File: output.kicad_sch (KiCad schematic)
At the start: 40 parts, among them J1 SMA, J2 SMA, J3 SMA, J4 SMA, T1 MABA-007159-000000, T2 MABA-007159-000000, U11 74LVC1G240, U12 74LVC1G125, U13 TS5A63157DBV

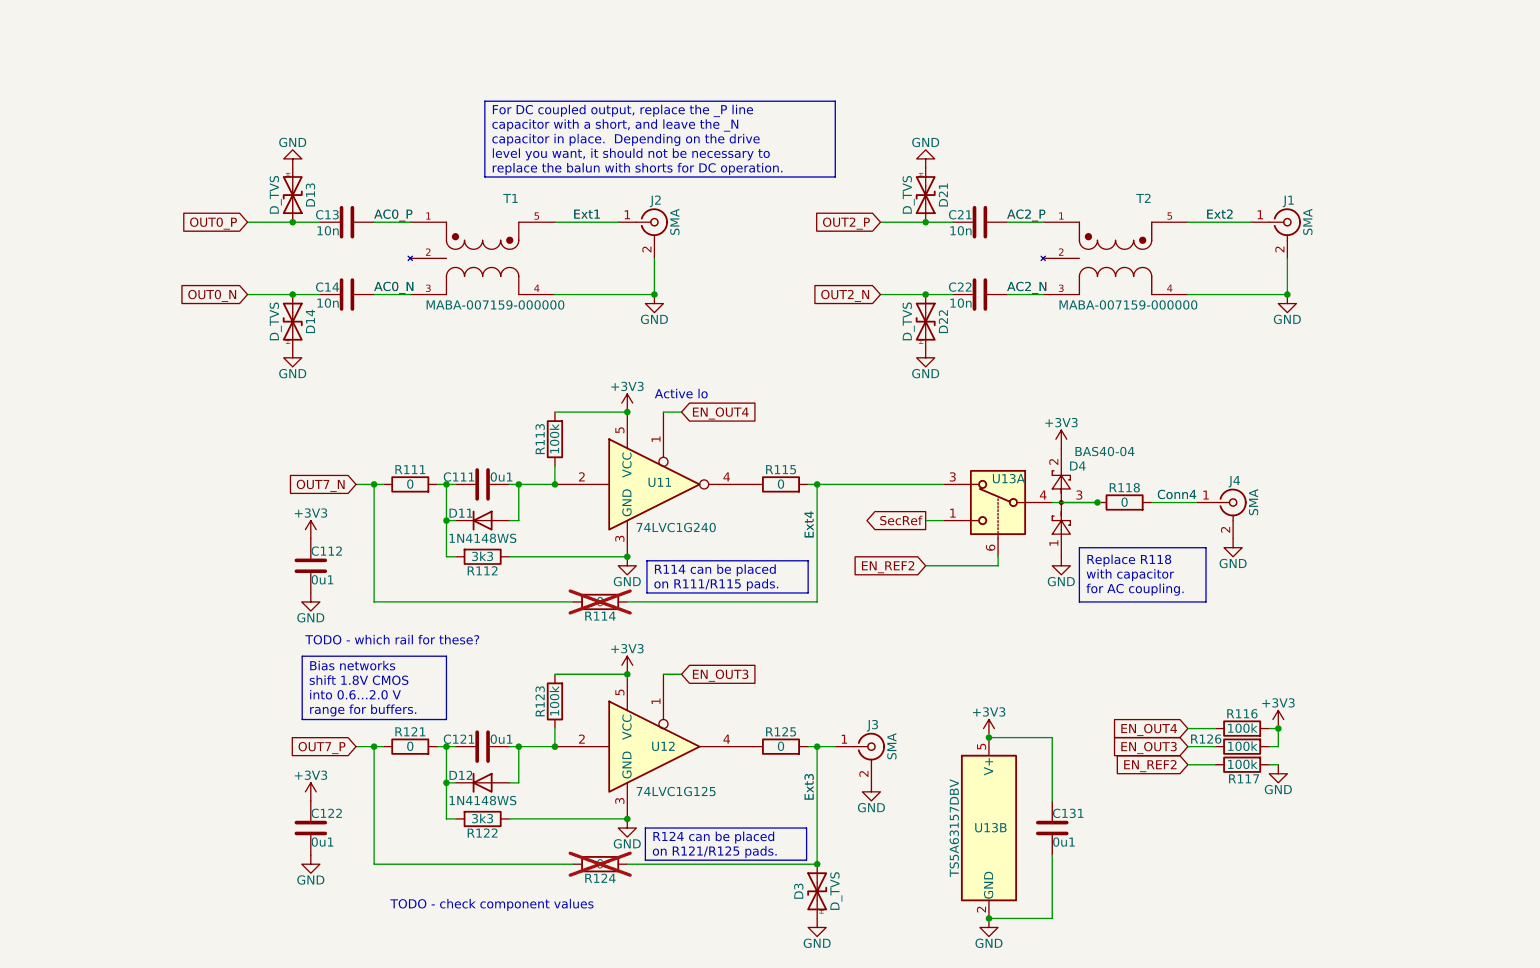
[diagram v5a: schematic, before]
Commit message: Supercap is back
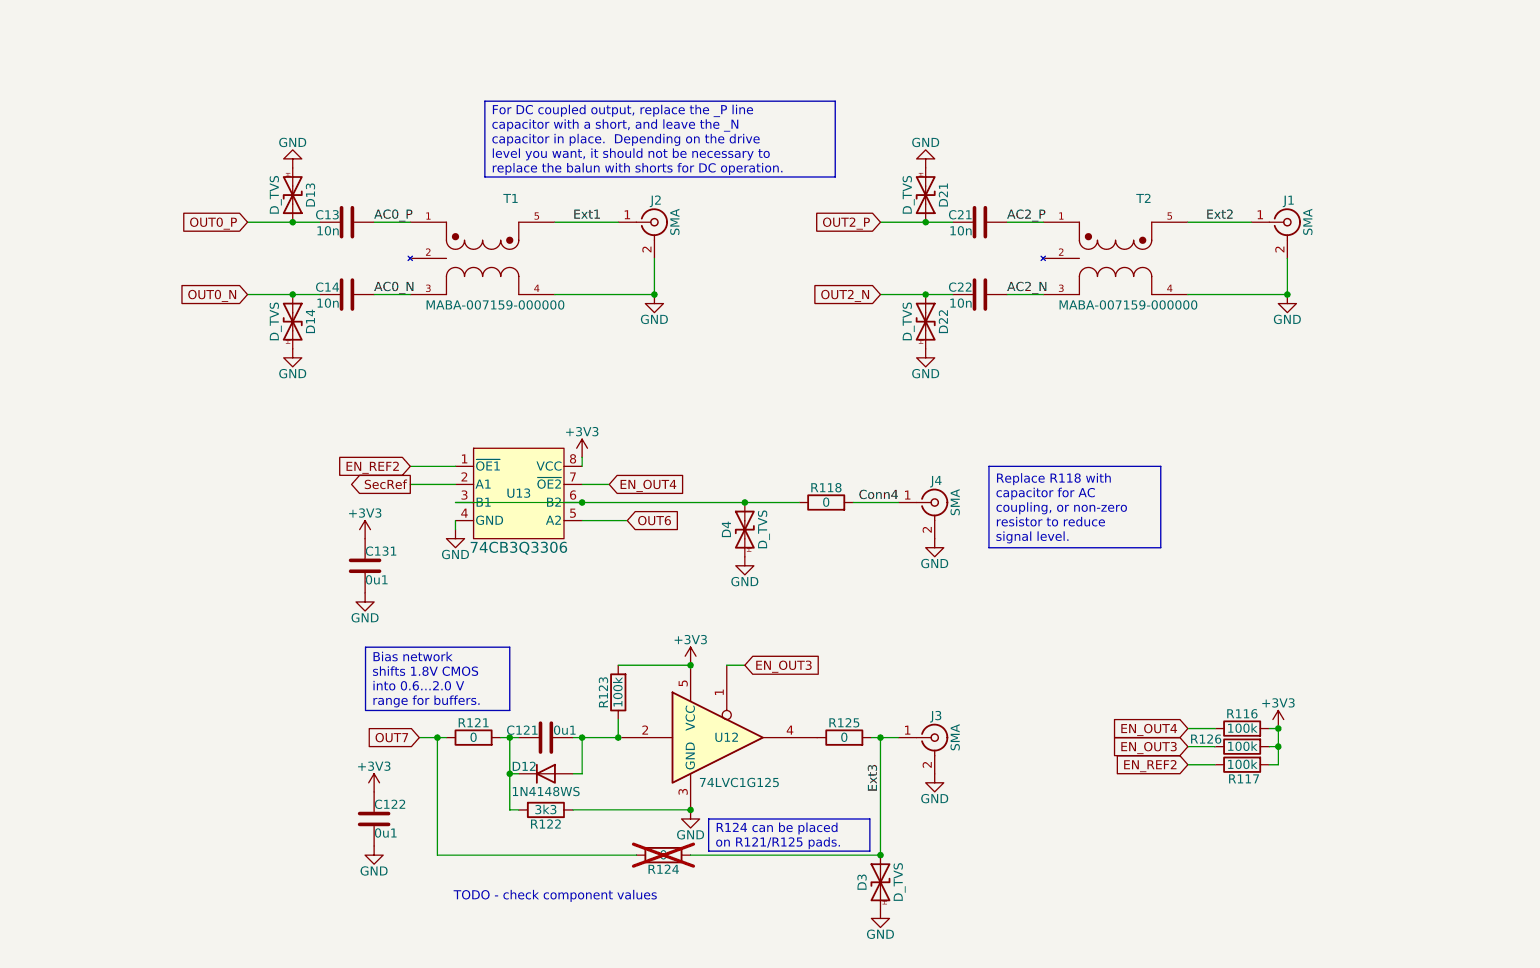
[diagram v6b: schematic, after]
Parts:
- removed C111, C112: 0u1, Capacitor_SMD:C_0402_1005Metric, symbol Device:C
- removed D11: 1N4148WS, Diode_SMD:D_SOD-323, symbol Diode:1N4148WS
- removed D4: BAS40-04, Package_TO_SOT_SMD:SOT-23, symbol Diode:BAS40-04
- removed R111, R114, R115: 0, Resistor_SMD:R_0603_1608Metric, symbol Device:R
- removed R112: 3k3, Resistor_SMD:R_0402_1005Metric, symbol Device:R
- removed R113: 100k, Resistor_SMD:R_0402_1005Metric, symbol Device:R
- removed U11: 74LVC1G240, Package_TO_SOT_SMD:SOT-23-5, symbol 74xGxx:74LVC1G240
- removed unit 2 of U13
- added D4: D_TVS, Parts:HHS_0402, symbol Parts:D_TVS
- U13: value TS5A63157DBV -> 74CB3Q3306; footprint Package_TO_SOT_SMD:SOT-23-6 -> Package_SO:VSSOP-8_2.3x2mm_P0.5mm; symbol Analog_Switch:TS5A63157DBV -> Parts:74CB3Q3306; now in the parts list
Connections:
- net Ext4 is gone; now on an unnamed net: U13.3 (B1)
- net +3V3: now also R117.2, U13.8 (VCC)
- net EN_OUT4: now also U13.7 (~{OE2})
- net EN_REF2: now also U13.1 (~{OE1}); no longer U13.6
- net GND: now also U13.4 (GND), D4.2 (A2); no longer R117.2
- net SecRef: now also U13.2 (A1); no longer U13.1
- net at R118.1: now also U13.6 (B2), D4.1 (A1); no longer U13.4
- net OUT7_P renamed OUT7
- new net OUT6: U13.5 (A2)
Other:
- note removed: "Active lo"
- note removed: "TODO - which rail for these?"
- moved on the sheet: C121, C122, C131, D12, D3, J3, J4, R118, R121, R122, R123, R124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

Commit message: Down to the dregs and clean-ups.
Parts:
- C13, C14, C21, C22: JLCPCB (none) -> C15195
- C76: renamed from C131; JLCPCB (none) -> C307331
- C77: renamed from C122; JLCPCB (none) -> C307331
- C78: renamed from C121; JLCPCB (none) -> C307331
- D12: JLCPCB (none) -> C2128
- D13, D14, D21, D22, D3, D4, U13: now left out of the parts list
- R74: renamed from R121; JLCPCB (none) -> C21189
- R75: renamed from R118; JLCPCB (none) -> C21189
- R76: renamed from R122; JLCPCB (none) -> C25890
- R77: renamed from R123; JLCPCB (none) -> C25741
- R78: renamed from R125; JLCPCB (none) -> C21189
- R79: renamed from R116; JLCPCB (none) -> C25741
- R80: renamed from R126; JLCPCB (none) -> C25741
- R84: renamed from R117; JLCPCB (none) -> C25741
- T1, T2: JLCPCB (none) -> C350943
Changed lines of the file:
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@@
 		(on_board yes)
 		(dnp no)
-		(property "Reference" "C121"
+		(property "Reference" "C78"
 			(at 128.524 125.476 90)
 			(effects
@@
 			)
 		)
-		(property "JLCPCB" ""
+		(property "JLCPCB" "C307331"
 			(at 129.54 125.73 0)
 			(effects
@@
 			(project "gpsref"
 				(path "/3160ff17-81c2-4674-af97-e8d9acaf6b65/26994282-45a2-461a-b033-dde2ded4d8ff"
-					(reference "C121")
+					(reference "C78")
 					(unit 1)
 				)
@@
 		(unit 1)
 		(exclude_from_sim no)
-		(in_bom yes)
+		(in_bom no)
 		(on_board yes)
 		(dnp no)
@@
 		(unit 1)
 		(exclude_from_sim no)
-		(in_bom yes)
+		(in_bom no)
 		(on_board yes)
 		(dnp no)
@@
 			)
 		)
-		(property "JLCPCB" ""
+		(property "JLCPCB" "C15195"
 			(at 101.6 53.34 0)
 			(effects
@@
 		(unit 1)
 		(exclude_from_sim no)
-		(in_bom yes)
+		(in_bom no)
 		(on_board yes)
 		(dnp no)
@@
 			)
 		)
-		(property "JLCPCB" ""
+		(property "JLCPCB" "C15195"
 			(at 190.5 63.5 0)
 			(effects
@@
 			)
 		)
+		(property "JLCPCB" "C350943"
+			(at 209.55 58.42 0)
+			(effects
+				(font
+					(size 1.27 1.27)
+				)
+				(hide yes)
+			)
+		)
 		(pin "3"
 		)
@@
 		(on_board yes)
 		(dnp no)
-		(property "Reference" "R122"
+		(property "Reference" "R76"
 			(at 129.54 137.922 90)
 			(effects
@@
 			)
 		)
-		(property "JLCPCB" ""
+		(property "JLCPCB" "C25890"
 			(at 129.54 135.89 0)
 			(effects
@@
 			(project "gpsref"
 				(path "/3160ff17-81c2-4674-af97-e8d9acaf6b65/26994282-45a2-461a-b033-dde2ded4d8ff"
-					(reference "R122")
+					(reference "R76")
 					(unit 1)
 				)
@@
 			)
 		)
+		(property "JLCPCB" "C350943"
+			(at 120.65 58.42 0)
+			(effects
+				(font
+					(size 1.27 1.27)
+				)
+				(hide yes)
+			)
+		)
 		(pin "3"
 		)
@@
 		(on_board yes)
 		(dnp no)
-		(property "Reference" "R117"
+		(property "Reference" "R84"
 			(at 227.584 131.572 90)
 			(effects
@@
 			)
 		)
-		(property "Datasheet" "Not sure about value."
+		(property "Datasheet" "~"
 			(at 227.33 129.54 0)
 			(effects
@@
 			)
 		)
-		(property "JLCPCB" ""
+		(property "JLCPCB" "C25741"
 			(at 227.33 129.54 0)
 			(effects
@@
 			(project "gpsref"
 				(path "/3160ff17-81c2-4674-af97-e8d9acaf6b65/26994282-45a2-461a-b033-dde2ded4d8ff"
-					(reference "R117")
+					(reference "R84")
 					(unit 1)
 				)
@@
 		(on_board yes)
 		(dnp no)
-		(property "Reference" "C122"
+		(property "Reference" "C77"
 			(at 105.41 135.89 0)
 			(effects
@@
 			)
 		)
+		(property "JLCPCB" "C307331"
+			(at 105.41 137.16 0)
+			(effects
+				(font
+					(size 1.27 1.27)
+				)
+				(hide yes)
+			)
+		)
 		(pin "1"
 		)
@@
 			(project "gpsref"
 				(path "/3160ff17-81c2-4674-af97-e8d9acaf6b65/26994282-45a2-461a-b033-dde2ded4d8ff"
-					(reference "C122")
+					(reference "C77")
 					(unit 1)
 				)
@@
 		(on_board yes)
 		(dnp no)
-		(property "Reference" "R125"
+		(property "Reference" "R78"
 			(at 171.45 123.698 90)
 			(effects
@@
 			)
 		)
-		(property "Datasheet" "Not sure about value."
+		(property "Datasheet" "~"
 			(at 171.45 125.73 0)
 			(effects
@@
 			)
 		)
-		(property "JLCPCB" ""
+		(property "JLCPCB" "C21189"
 			(at 171.45 125.73 0)
 			(effects
@@
 			(project "gpsref"
 				(path "/3160ff17-81c2-4674-af97-e8d9acaf6b65/26994282-45a2-461a-b033-dde2ded4d8ff"
-					(reference "R125")
+					(reference "R78")
 					(unit 1)
 				)
@@
 		(unit 1)
 		(exclude_from_sim no)
-		(in_bom yes)
+		(in_bom no)
 		(on_board yes)
 		(dnp no)
@@
 		(on_board yes)
 		(dnp no)
-		(property "Reference" "R116"
+		(property "Reference" "R79"
 			(at 227.33 122.428 90)
 			(effects
@@
 			)
 		)
-		(property "Datasheet" "Not sure about value."
+		(property "Datasheet" "~"
 			(at 227.33 124.46 0)
 			(effects
@@
 			)
 		)
-		(property "JLCPCB" ""
+		(property "JLCPCB" "C25741"
 			(at 227.33 124.46 0)
 			(effects
@@
 			(project "gpsref"
 				(path "/3160ff17-81c2-4674-af97-e8d9acaf6b65/26994282-45a2-461a-b033-dde2ded4d8ff"
-					(reference "R116")
+					(reference "R79")
 					(unit 1)
 				)
@@
 			)
 		)
-		(property "JLCPCB" ""
+		(property "JLCPCB" "C15195"
 			(at 101.6 63.5 0)
 			(effects
@@
 		(on_board yes)
 		(dnp no)
-		(property "Reference" "C131"
+		(property "Reference" "C76"
 			(at 104.14 100.33 0)
 			(effects
@@
 			)
 		)
+		(property "JLCPCB" "C307331"
+			(at 104.14 101.6 0)
+			(effects
+				(font
+					(size 1.27 1.27)
+				)
+				(hide yes)
+			)
+		)
 		(pin "1"
 		)
@@
 			(project "gpsref"
 				(path "/3160ff17-81c2-4674-af97-e8d9acaf6b65/26994282-45a2-461a-b033-dde2ded4d8ff"
-					(reference "C131")
+					(reference "C76")
 					(unit 1)
 				)
@@
 		(unit 1)
 		(exclude_from_sim no)
-		(in_bom yes)
+		(in_bom no)
 		(on_board yes)
 		(dnp no)
@@
 		(unit 1)
 		(exclude_from_sim no)
-		(in_bom yes)
+		(in_bom no)
 		(on_board yes)
 		(dnp no)
@@
 		(on_board yes)
 		(dnp no)
-		(property "Reference" "R118"
+		(property "Reference" "R75"
 			(at 168.91 90.678 90)
 			(effects
@@
 			)
 		)
-		(property "Datasheet" "Not sure about value."
+		(property "Datasheet" "~"
 			(at 168.91 92.71 0)
 			(effects
@@
 			)
 		)
-		(property "JLCPCB" ""
+		(property "JLCPCB" "C21189"
 			(at 168.91 92.71 0)
 			(effects
@@
 			(project "gpsref"
 				(path "/3160ff17-81c2-4674-af97-e8d9acaf6b65/26994282-45a2-461a-b033-dde2ded4d8ff"
-					(reference "R118")
+					(reference "R75")
 					(unit 1)
 				)
@@
 		(unit 1)
 		(exclude_from_sim no)
-		(in_bom yes)
+		(in_bom no)
 		(on_board yes)
 		(dnp no)
@@
 		(on_board yes)
 		(dnp no)
-		(property "Reference" "R121"
+		(property "Reference" "R74"
 			(at 119.38 123.698 90)
 			(effects
@@
 			)
 		)
-		(property "Datasheet" "Not sure about value."
+		(property "Datasheet" "~"
 			(at 119.38 125.73 0)
 			(effects
@@
 			)
 		)
-		(property "JLCPCB" ""
+		(property "JLCPCB" "C21189"
 			(at 119.38 125.73 0)
 			(effects
@@
 			(project "gpsref"
 				(path "/3160ff17-81c2-4674-af97-e8d9acaf6b65/26994282-45a2-461a-b033-dde2ded4d8ff"
-					(reference "R121")
+					(reference "R74")
 					(unit 1)
 				)
@@
 			)
 		)
-		(property "JLCPCB" ""
+		(property "JLCPCB" "C15195"
 			(at 190.5 53.34 0)
 			(effects
@@
 		(on_board yes)
 		(dnp no)
-		(property "Reference" "R123"
+		(property "Reference" "R77"
 			(at 137.668 119.38 90)
 			(effects
@@
 			)
 		)
-		(property "Datasheet" "Not sure about value."
+		(property "Datasheet" "~"
 			(at 139.7 119.38 0)
 			(effects
@@
 			)
 		)
-		(property "JLCPCB" ""
+		(property "JLCPCB" "C25741"
 			(at 139.7 119.38 0)
 			(effects
@@
 			(project "gpsref"
 				(path "/3160ff17-81c2-4674-af97-e8d9acaf6b65/26994282-45a2-461a-b033-dde2ded4d8ff"
-					(reference "R123")
+					(reference "R77")
 					(unit 1)
 				)
@@
 			)
 		)
+		(property "JLCPCB" "C2128"
+			(at 129.54 130.81 0)
+			(effects
+				(font
+					(size 1.27 1.27)
+				)
+				(hide yes)
+			)
+		)
 		(pin "2"
 		)
@@
 		(on_board yes)
 		(dnp no)
-		(property "Reference" "R126"
+		(property "Reference" "R80"
 			(at 222.25 125.984 90)
 			(effects
@@
 			)
 		)
-		(property "Datasheet" "Not sure about value."
+		(property "Datasheet" "~"
 			(at 227.33 127 0)
 			(effects
@@
 			)
 		)
-		(property "JLCPCB" ""
+		(property "JLCPCB" "C25741"
 			(at 227.33 127 0)
 			(effects
@@
 			(project "gpsref"
 				(path "/3160ff17-81c2-4674-af97-e8d9acaf6b65/26994282-45a2-461a-b033-dde2ded4d8ff"
-					(reference "R126")
+					(reference "R80")
 					(unit 1)
 				)

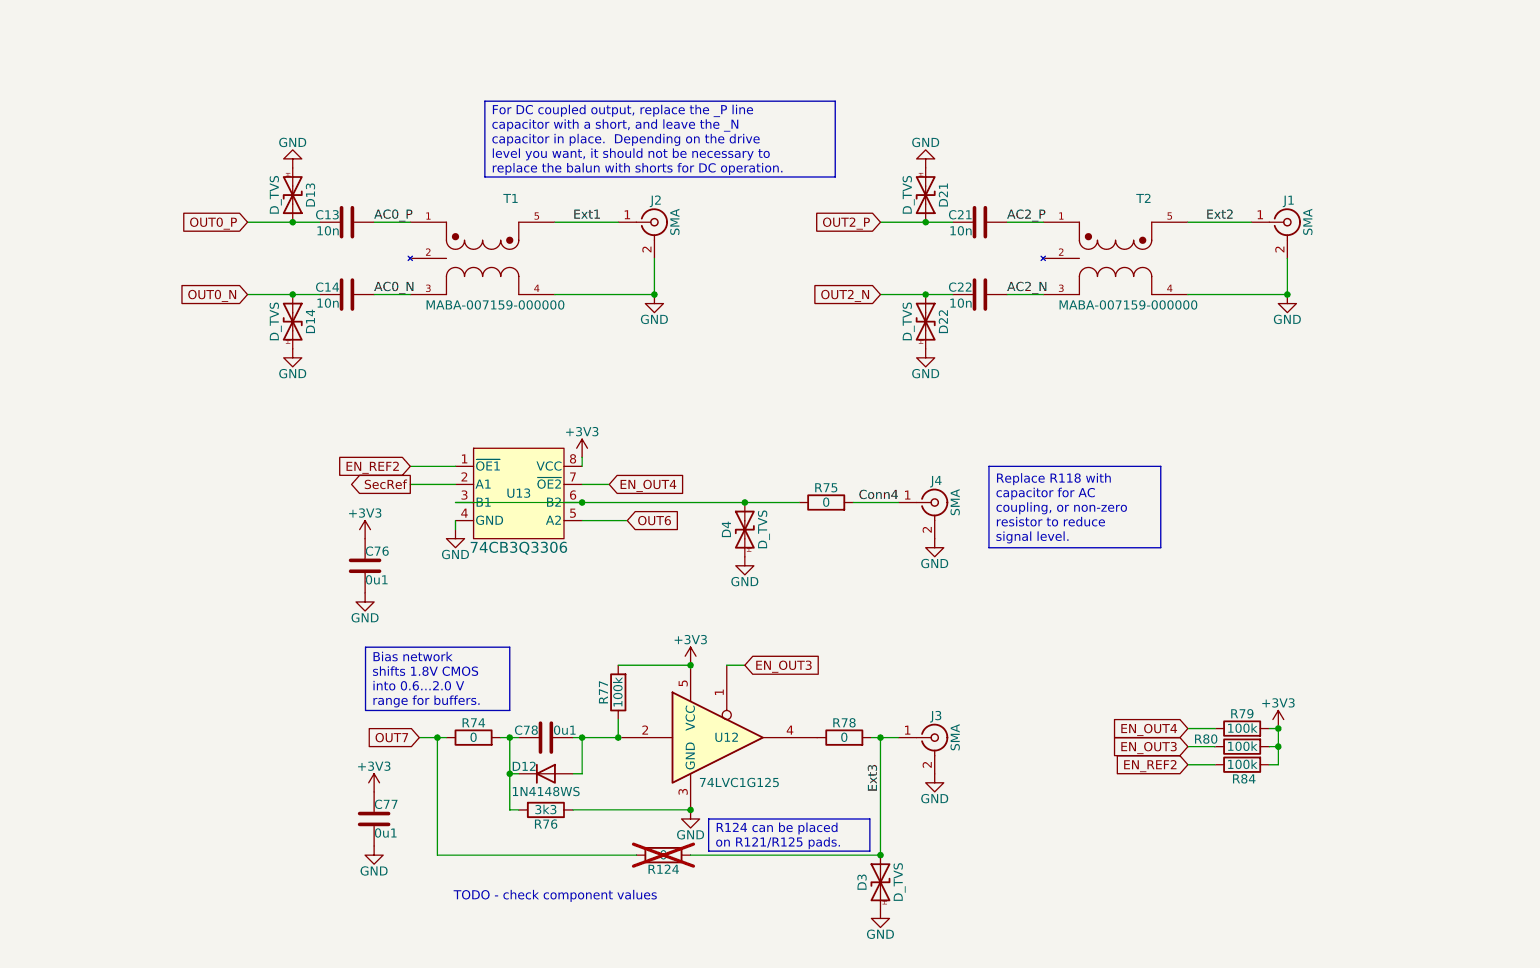
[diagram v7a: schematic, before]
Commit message: Add a U.Fl connector for fun.
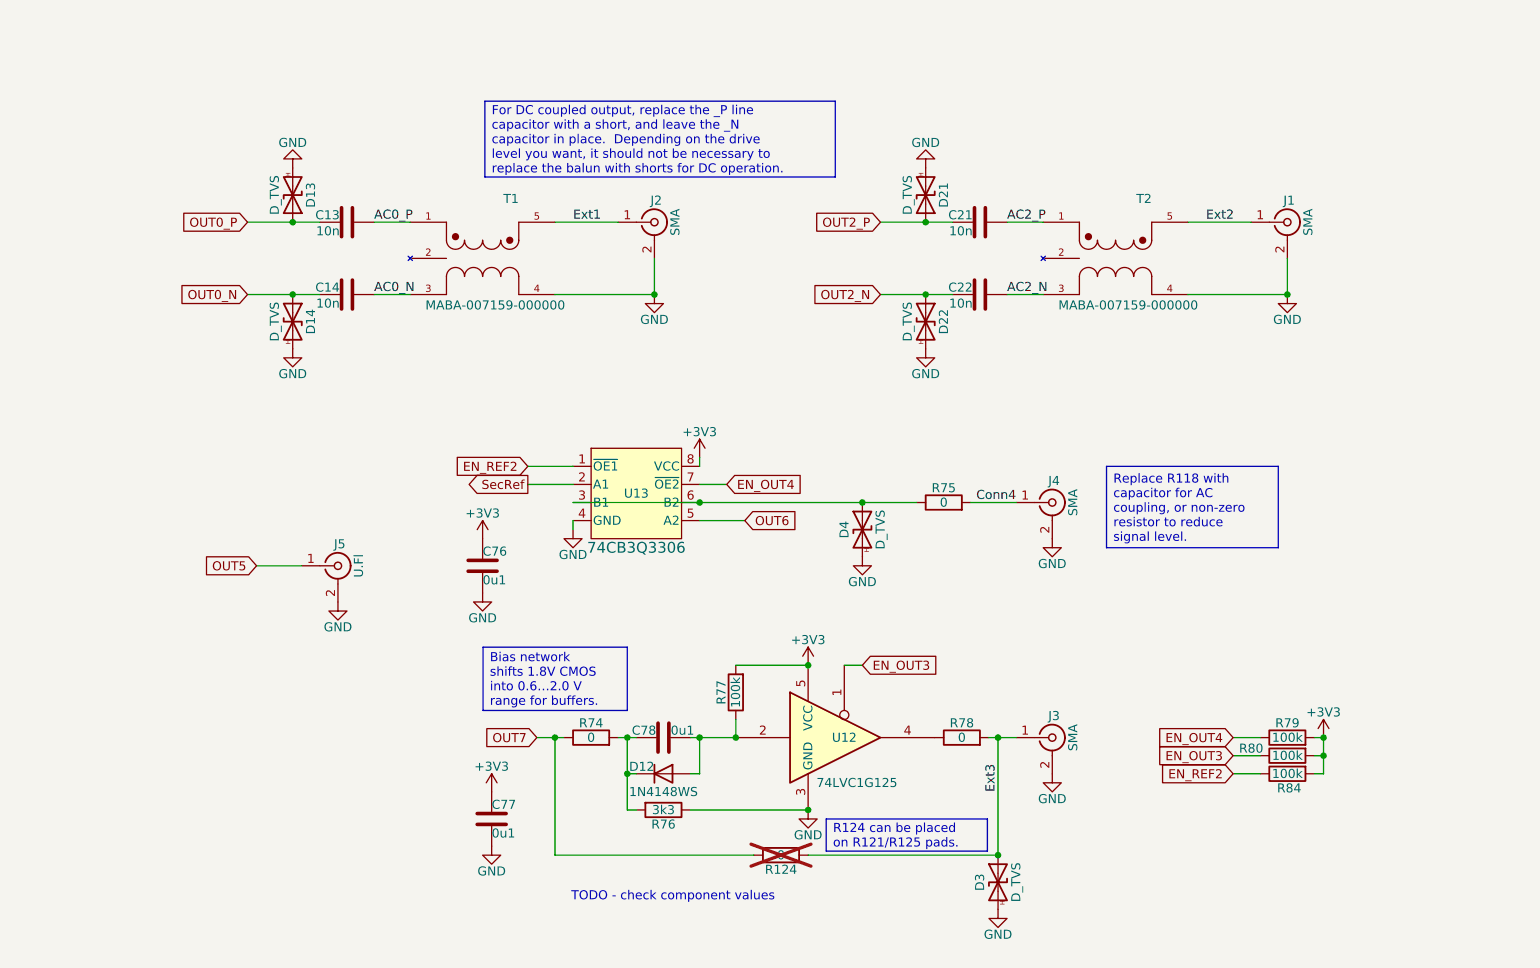
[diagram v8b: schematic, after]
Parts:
- added J5: U.Fl, Connector_Coaxial:U.FL_Hirose_U.FL-R-SMT-1_Vertical, symbol Connector:Conn_Coaxial
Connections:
- net GND: now also J5.2 (Ext)
- new net OUT5: J5.1 (In)
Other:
- moved on the sheet: C76, C77, C78, D12, D3, D4, J3, J4, R124, R74, R75, R76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
